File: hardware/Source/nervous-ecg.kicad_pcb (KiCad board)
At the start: 2 copper layers, 26 x 40 mm, 65 parts, among them J1 CONN RCP USB3.1 TYPEC 24P SMD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, J2 MOLEX 53048-0310, J3 CONN HEADER R/A 4POS 2.54MM, U1 RF TXRX MODULE BT TRACE ANT S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, U2 IC BATT CHG LI-ION 1CELL 16QFN, U3 IC BATT FUEL GAUGE LICOO2 12S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, U4 IC REG LINEAR 3.3V 200MA SOT2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, U5 IC ECG FRONT END 20LFCSP, U6 IC INTFACE SPECIALIZED TSOT23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, U7 SWITCH TACTILE SPST-NO 0.02A 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

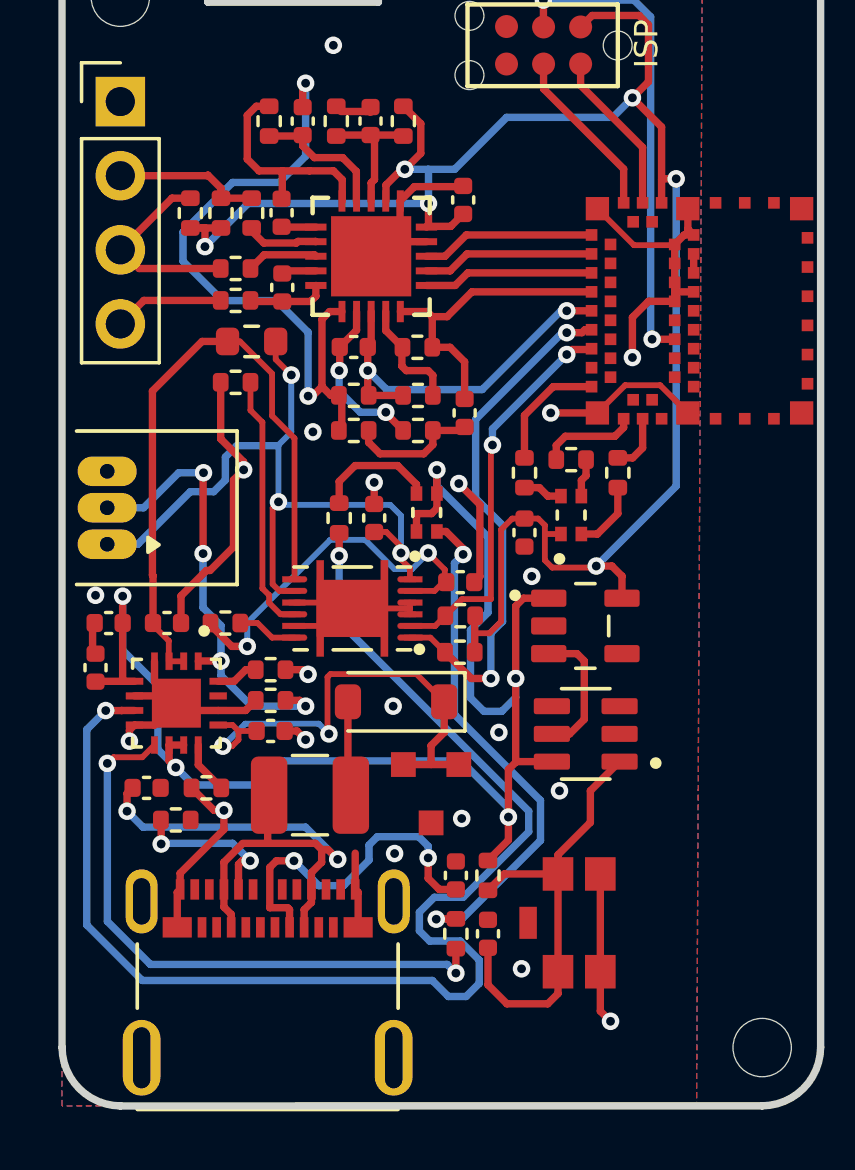
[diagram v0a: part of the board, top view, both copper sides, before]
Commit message: fix : readjustment of decoupling capacitors positioning
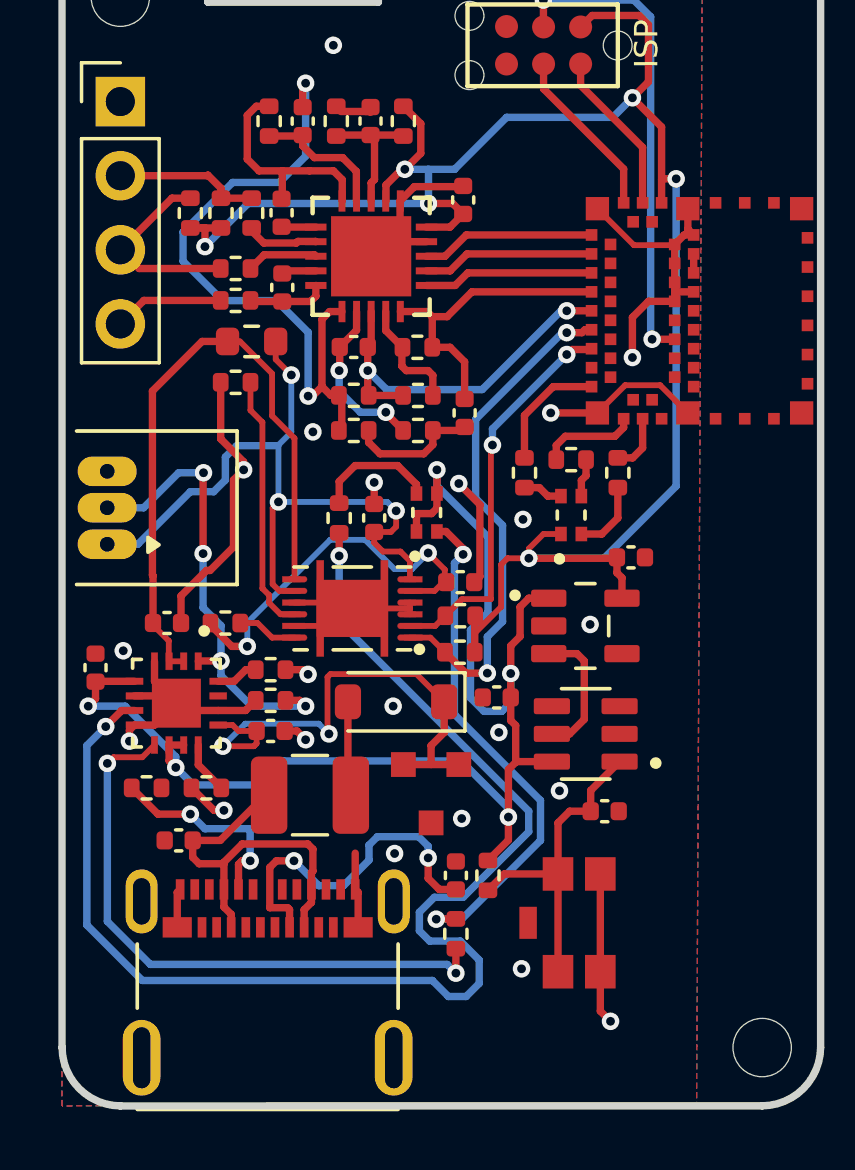
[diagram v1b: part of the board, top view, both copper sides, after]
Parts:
- moved C8 13.5 mm to (44.9, 50.0)
- moved C13 5.80 mm to (48.6, 53.9), turned to 0 degrees
- moved C9 3.75 mm to (49.5, 45.2), turned to 0 degrees
- moved C2 2.11 mm to (34.0, 54.9), turned to 180 degrees
- moved R28 1.49 mm to (32.9, 53.1)
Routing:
- net VBUS: track 20.0 -> 13.5 mm, vias 2 -> 0
- net GND: track 71.4 -> 66.9 mm, vias 20 -> 21
- net Net-(U6-IN): track 15.5 -> 11.1 mm
- net VSYS: track 50.9 -> 46.5 mm
- net Net-(J1-CC1): track 5.44 -> 7.12 mm
- net VCC: track 63.2 -> 64.3 mm
- net Net-(D1-K): track 17.1 -> 17.8 mm

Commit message: fix: update board revision
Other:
- board text added: "NERVOUS ECG Sensor v1.0.1 RENFORCE-ANR-22-CE31-0023-03 (c) 2024 INSA Lyon, CNRS"
- board text removed: "NERVOUS ECG Sensor v1.0 RENFORCE-ANR-22-CE31-0023-03 (c) 2024 INSA Lyon, CNRS"
